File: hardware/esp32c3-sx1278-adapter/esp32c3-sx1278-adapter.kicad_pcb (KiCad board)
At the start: 2 copper layers, 24 x 58 mm, 5 parts, among them J1 Conn_01x08, J2 Conn_01x08, J3 Antenna, J4 SMA, U2 SX1278_module

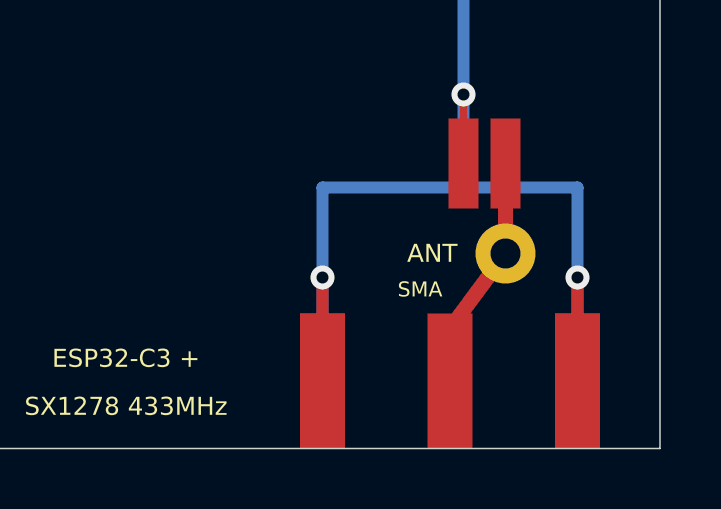
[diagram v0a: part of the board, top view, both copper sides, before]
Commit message: Add the green D-Sun CC1101 board with the same assets as the blue E07-M1101D
The user's second CC1101 board ("433MHz D-Sun CC1101", green; EasyEDA calls
it RF1101SE V3.1) carries the same eight signals on the same 2x4 header,
with the GND/VCC column in the same place but the three signal columns
permuted, so it does not fit the socket adapter's pinout and is supported
with jumper wires instead.

* scripts/generate_dsun.py -> hardware/parts/cc1101-dsun: outline 14.4 x
  30, header rows 2.1 / 4.6 from the edge, columns 2.9..10.5 from the left
  long edge, two 1.8 mm holes beside the SMA jack, pin names on both sides
  and the original's back-side legend grid.  Dimensions measured from the
  user's photos with the E07-M1101D as the scale (+/- 0.3 mm).
* 3D models (cc1101-dsun.step, -components.step) attached to the board.
* Pinout diagram: third column, green, with the back legend; wiring diagram
  docs/images/wiring-cc1101-dsun.svg (its wires cannot all nest; the chip
  select runs along the back of the board below the header).
* README: comparison table with the blue board, why the socket does not
  take it, a component-board section, 3D model row; CI regenerates it and
  the manufacturing notes cover it.

The photos also showed both boards' edge-mount SMA jacks have their ground
legs 5.5 mm apart, not 8.5: the shared SMA footprint, the E07 reference
board, the SX1278 adapter's SMA ground routing (now skirting the antenna
wire hole) and the 3D jack model follow.

Strap change for the jumper-wire builds: the SuperMini has one G pin (the
brown wire's), so the Ra-02's strap wire goes from GPIO5 to GPIO4, which
firmware drives low while reading the strap; documented with the read
procedure.

Co-Authored-By: Claude Fable 5.1 <noreply@anthropic.com>
Claude-Session: https://claude.ai/code/session_01JoGdh4Cg3VtTTDZi4gQuiN
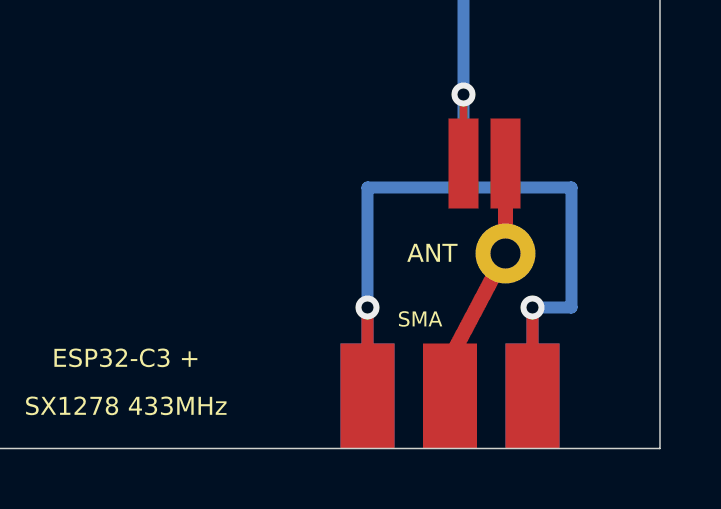
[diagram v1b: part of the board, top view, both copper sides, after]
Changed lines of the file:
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@@
 		(sheetfile "esp32c3-sx1278-adapter.kicad_sch")
 		(property "Reference" "J4"
-			(at 0 -5.5 0)
+			(at 0 -4.5 0)
 			(layer "F.SilkS")
 			(hide yes)
@@
 		(attr smd)
 		(fp_rect
-			(start -5.25 -4.75)
-			(end 5.25 0.25)
+			(start -3.9 -3.75)
+			(end 3.9 0.25)
 			(stroke
 				(width 0.05)
@@
 		)
 		(fp_text user "${REFERENCE}"
-			(at 0 -5.5 0)
+			(at 0 -4.5 0)
 			(layer "F.Fab")
 			(effects
@@
 		)
 		(pad "1" smd rect
-			(at 0 -2.25)
-			(size 1.5 4.5)
+			(at 0 -1.75)
+			(size 1.8 3.5)
 			(layers "F.Cu" "F.Mask" "F.Paste")
 			(net 20 "ANT")
@@
 		)
 		(pad "2" smd rect
-			(at -4.25 -2.25)
-			(size 1.5 4.5)
+			(at -2.75 -1.75)
+			(size 1.8 3.5)
 			(layers "F.Cu" "F.Mask" "F.Paste")
 			(net 10 "GND")
@@
 		)
 		(pad "2" smd rect
-			(at -4.25 -2.25)
-			(size 1.5 4.5)
+			(at -2.75 -1.75)
+			(size 1.8 3.5)
 			(layers "B.Cu" "B.Mask" "B.Paste")
 			(net 10 "GND")
@@
 		)
 		(pad "2" smd rect
-			(at 4.25 -2.25)
-			(size 1.5 4.5)
+			(at 2.75 -1.75)
+			(size 1.8 3.5)
 			(layers "F.Cu" "F.Mask" "F.Paste")
 			(net 10 "GND")
@@
 		)
 		(pad "2" smd rect
-			(at 4.25 -2.25)
-			(size 1.5 4.5)
+			(at 2.75 -1.75)
+			(size 1.8 3.5)
 			(layers "B.Cu" "B.Mask" "B.Paste")
 			(net 10 "GND")
@@
 	)
 	(gr_text "SMA"
-		(at 116 152.7 0)
+		(at 116 153.7 0)
 		(layer "F.SilkS")
 		(effects
@@
 	(segment
 		(start 118.85 151.5)
-		(end 117 154)
+		(end 117 155)
 		(width 0.5)
 		(layer "F.Cu")
@@
 	)
 	(segment
-		(start 117 154)
-		(end 117 155.75)
+		(start 117 155)
+		(end 117 156.25)
 		(width 0.5)
 		(layer "F.Cu")
@@
 	(segment
 		(start 117.45 149.3)
-		(end 121.25 149.3)
-		(width 0.4)
-		(layer "B.Cu")
-		(net 10)
-	)
-	(segment
-		(start 121.25 149.3)
-		(end 121.25 155.75)
+		(end 121.05 149.3)
+		(width 0.4)
+		(layer "B.Cu")
+		(net 10)
+	)
+	(segment
+		(start 121.05 149.3)
+		(end 121.05 153.3)
+		(width 0.4)
+		(layer "B.Cu")
+		(net 10)
+	)
+	(segment
+		(start 121.05 153.3)
+		(end 119.75 153.3)
+		(width 0.4)
+		(layer "B.Cu")
+		(net 10)
+	)
+	(segment
+		(start 119.75 153.3)
+		(end 119.75 156.25)
 		(width 0.4)
 		(layer "B.Cu")
@@
 	(segment
 		(start 117.45 149.3)
-		(end 112.75 149.3)
-		(width 0.4)
-		(layer "B.Cu")
-		(net 10)
-	)
-	(segment
-		(start 112.75 149.3)
-		(end 112.75 155.75)
-		(width 0.4)
-		(layer "B.Cu")
-		(net 10)
-	)
-	(segment
-		(start 112.75 152.3)
-		(end 112.75 155.75)
-		(width 0.4)
-		(layer "F.Cu")
-		(net 10)
-	)
-	(segment
-		(start 121.25 152.3)
-		(end 121.25 155.75)
+		(end 114.25 149.3)
+		(width 0.4)
+		(layer "B.Cu")
+		(net 10)
+	)
+	(segment
+		(start 114.25 149.3)
+		(end 114.25 156.25)
+		(width 0.4)
+		(layer "B.Cu")
+		(net 10)
+	)
+	(segment
+		(start 114.25 153.3)
+		(end 114.25 156.25)
+		(width 0.4)
+		(layer "F.Cu")
+		(net 10)
+	)
+	(segment
+		(start 119.75 153.3)
+		(end 119.75 156.25)
 		(width 0.4)
 		(layer "F.Cu")
@@
 	)
 	(via
-		(at 112.75 152.3)
+		(at 114.25 153.3)
 		(size 0.8)
 		(drill 0.4)
@@
 	)
 	(via
-		(at 121.25 152.3)
+		(at 119.75 153.3)
 		(size 0.8)
 		(drill 0.4)

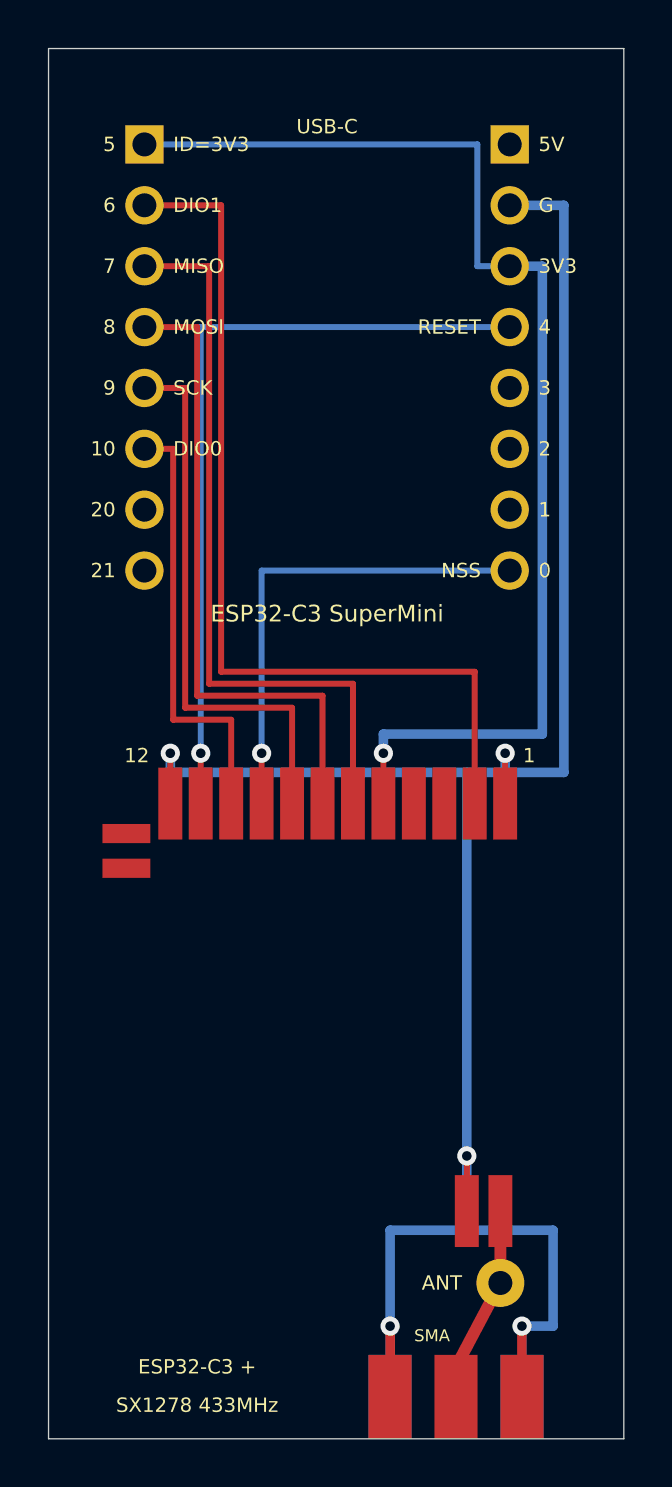
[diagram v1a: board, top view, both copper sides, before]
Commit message: Adapters: GPIO map that lets the same socket take all three radio boards
The green D-Sun CC1101 board plugs into the socket adapter's 2x4 socket
too; only its signal order differs, which the firmware absorbs with a pin
map per board.  What the hardware must guarantee is that no socket
position that carries a radio OUTPUT on any of the boards is an ESP32-C3
boot strapping pin (GPIO2/8/9).  Only position 4 (blue CSN, green SCK,
Ra-02 NSS) is an input on every board, so it takes GPIO9; GPIO8 moves to
the spare header and positions 5 and 6 are fed from GPIO3 and GPIO4.

Socket positions 3..8 are now GPIO10, 9, 3, 4, 7, 6.  Per-board maps:
blue E07 MOSI 4 SCK 3 CSN 9 MISO 7 GDO0 10 GDO2 6; green D-Sun MOSI 10
SCK 9 CSN 6 MISO 3 GDO0 7 GDO2 4; Ra-02 MOSI 4 SCK 3 NSS 9 MISO 7 RST 10
DIO0 6.  The README also describes telling the two CC1101 boards apart
passively at power-up (an unconfigured CC1101 clocks XOSC/192 out of
GDO0, on GPIO10 for the blue board and GPIO7 for the green).

Socket adapter routing, still entirely on the back copper: GPIO9 leaves
its pad sideways into the gap before GPIO10 and drops into position 4;
MISO takes the column under GPIO8's pad; SCK and MOSI come down from the
power row through the gaps either side of GPIO8's pad, and GPIO8 climbs
between them to the header (now 3V3, 8, 2, 1, 0, 21TX, 20RX).

SX1278 module adapter: same GPIOs with MOSI and SCK swapped (GPIO3/4) so
its bottom copper nests, NSS on GPIO9 via the top-copper bus, RESET on
GPIO8 (an ESP32 output).

Jumper-wire diagrams: one layout serves all three boards; GPIO4 and GPIO3
take the ribbon's white and black; the Ra-02 strap goes to GPIO1 (GPIO4
is now MOSI).  Both adapters pass ERC and DRC.

Co-Authored-By: Claude Fable 5.1 <noreply@anthropic.com>
Claude-Session: https://claude.ai/code/session_01JoGdh4Cg3VtTTDZi4gQuiN
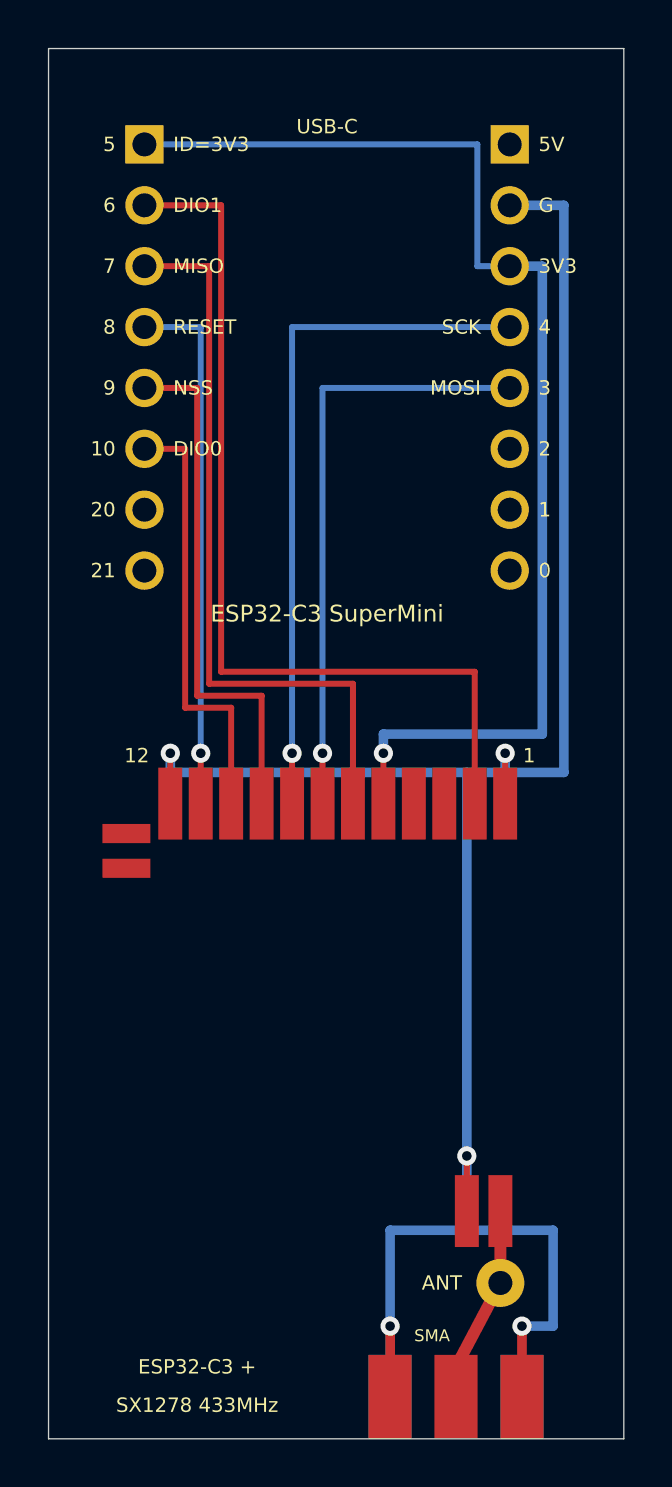
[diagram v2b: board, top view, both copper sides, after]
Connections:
- J1 pad 4: MOSI -> RESET
- J1 pad 5: SCK -> NSS
- J2 pad 4: RESET -> SCK
- J2 pad 5: GPIO3 -> MOSI
- J2 pad 8: NSS -> GPIO0
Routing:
- net RESET: track 33.3 -> 22.7 mm
- net SCK: track 24.0 -> 29.5 mm, vias 0 -> 1
- net NSS: track 20.6 -> 22.7 mm, vias 1 -> 0
- net MOSI: track 27.8 -> 25.6 mm, vias 0 -> 1
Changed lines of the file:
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@@
 	(net 2 "DIO1")
 	(net 3 "MISO")
-	(net 4 "MOSI")
-	(net 5 "SCK")
+	(net 4 "RESET")
+	(net 5 "NSS")
 	(net 6 "DIO0")
 	(net 7 "GPIO20")
@@
 	(net 9 "+5V")
 	(net 10 "GND")
-	(net 11 "RESET")
-	(net 12 "GPIO3")
+	(net 11 "SCK")
+	(net 12 "MOSI")
 	(net 13 "GPIO2")
 	(net 14 "GPIO1")
-	(net 15 "NSS")
+	(net 15 "GPIO0")
 	(net 16 "DIO2")
 	(net 17 "DIO3")
@@
 			(layers "*.Cu" "*.Mask")
 			(remove_unused_layers no)
-			(net 4 "MOSI")
+			(net 4 "RESET")
 			(pinfunction "Pin_4")
 			(pintype "passive")
@@
 			(layers "*.Cu" "*.Mask")
 			(remove_unused_layers no)
-			(net 5 "SCK")
+			(net 5 "NSS")
 			(pinfunction "Pin_5")
 			(pintype "passive")
@@
 			(layers "*.Cu" "*.Mask")
 			(remove_unused_layers no)
-			(net 11 "RESET")
+			(net 11 "SCK")
 			(pinfunction "Pin_4")
 			(pintype "passive")
@@
 			(layers "*.Cu" "*.Mask")
 			(remove_unused_layers no)
-			(net 12 "GPIO3")
+			(net 12 "MOSI")
 			(pinfunction "Pin_5")
 			(pintype "passive")
@@
 			(layers "*.Cu" "*.Mask")
 			(remove_unused_layers no)
-			(net 15 "NSS")
+			(net 15 "GPIO0")
 			(pinfunction "Pin_8")
 			(pintype "passive")
@@
 			(size 1 3)
 			(layers "F.Cu" "F.Mask" "F.Paste")
-			(net 4 "MOSI")
+			(net 12 "MOSI")
 			(pinfunction "Pin_7")
 			(pintype "passive")
@@
 			(size 1 3)
 			(layers "F.Cu" "F.Mask" "F.Paste")
-			(net 5 "SCK")
+			(net 11 "SCK")
 			(pinfunction "Pin_8")
 			(pintype "passive")
@@
 			(size 1 3)
 			(layers "F.Cu" "F.Mask" "F.Paste")
-			(net 15 "NSS")
+			(net 5 "NSS")
 			(pinfunction "Pin_9")
 			(pintype "passive")
@@
 			(size 1 3)
 			(layers "F.Cu" "F.Mask" "F.Paste")
-			(net 11 "RESET")
+			(net 4 "RESET")
 			(pinfunction "Pin_11")
 			(pintype "passive")
@@
 		)
 	)
-	(gr_text "MOSI"
+	(gr_text "RESET"
 		(at 105.2 111.62 0)
 		(layer "F.SilkS")
@@
 		)
 	)
-	(gr_text "SCK"
+	(gr_text "NSS"
 		(at 105.2 114.16 0)
 		(layer "F.SilkS")
@@
 		)
 	)
-	(gr_text "RESET"
+	(gr_text "SCK"
 		(at 118.04 111.62 0)
 		(layer "F.SilkS")
@@
 		)
 	)
+	(gr_text "MOSI"
+		(at 118.04 114.16 0)
+		(layer "F.SilkS")
+		(effects
+			(font
+				(size 0.6 0.6)
+				(thickness 0.09)
+			)
+			(justify right)
+		)
+	)
 	(gr_text "2"
 		(at 120.44 116.7 0)
@@
 		)
 	)
-	(gr_text "NSS"
-		(at 118.04 121.78 0)
-		(layer "F.SilkS")
-		(effects
-			(font
-				(size 0.6 0.6)
-				(thickness 0.09)
-			)
-			(justify right)
-		)
-	)
 	(gr_text "ANT"
 		(at 117.25 151.5 0)
@@
 	)
 	(segment
-		(start 104 111.62)
-		(end 106.2 111.62)
-		(width 0.25)
-		(layer "F.Cu")
-		(net 4)
-	)
-	(segment
-		(start 106.2 111.62)
+		(start 104 114.16)
+		(end 106.2 114.16)
+		(width 0.25)
+		(layer "F.Cu")
+		(net 5)
+	)
+	(segment
+		(start 106.2 114.16)
 		(end 106.2 127)
 		(width 0.25)
 		(layer "F.Cu")
-		(net 4)
+		(net 5)
 	)
 	(segment
 		(start 106.2 127)
-		(end 111.43 127)
-		(width 0.25)
-		(layer "F.Cu")
-		(net 4)
-	)
-	(segment
-		(start 111.43 127)
-		(end 111.43 132)
-		(width 0.25)
-		(layer "F.Cu")
-		(net 4)
-	)
-	(segment
-		(start 104 114.16)
-		(end 105.7 114.16)
+		(end 108.89 127)
 		(width 0.25)
 		(layer "F.Cu")
@@
 	)
 	(segment
-		(start 105.7 114.16)
+		(start 108.89 127)
+		(end 108.89 132)
+		(width 0.25)
+		(layer "F.Cu")
+		(net 5)
+	)
+	(segment
+		(start 104 116.7)
+		(end 105.7 116.7)
+		(width 0.25)
+		(layer "F.Cu")
+		(net 6)
+	)
+	(segment
+		(start 105.7 116.7)
 		(end 105.7 127.5)
 		(width 0.25)
 		(layer "F.Cu")
-		(net 5)
+		(net 6)
 	)
 	(segment
 		(start 105.7 127.5)
-		(end 110.16 127.5)
-		(width 0.25)
-		(layer "F.Cu")
-		(net 5)
-	)
-	(segment
-		(start 110.16 127.5)
-		(end 110.16 132)
-		(width 0.25)
-		(layer "F.Cu")
-		(net 5)
-	)
-	(segment
-		(start 104 116.7)
-		(end 105.2 116.7)
+		(end 107.62 127.5)
 		(width 0.25)
 		(layer "F.Cu")
@@
 	)
 	(segment
-		(start 105.2 116.7)
-		(end 105.2 128)
-		(width 0.25)
-		(layer "F.Cu")
-		(net 6)
-	)
-	(segment
-		(start 105.2 128)
-		(end 107.62 128)
-		(width 0.25)
-		(layer "F.Cu")
-		(net 6)
-	)
-	(segment
-		(start 107.62 128)
+		(start 107.62 127.5)
 		(end 107.62 132)
 		(width 0.25)
@@
 	)
 	(segment
-		(start 119.24 111.62)
+		(start 104 111.62)
 		(end 106.35 111.62)
 		(width 0.25)
 		(layer "B.Cu")
-		(net 11)
+		(net 4)
 	)
 	(segment
@@
 		(width 0.25)
 		(layer "B.Cu")
-		(net 11)
+		(net 4)
 	)
 	(segment
@@
 		(width 0.25)
 		(layer "F.Cu")
+		(net 4)
+	)
+	(segment
+		(start 119.24 111.62)
+		(end 110.16 111.62)
+		(width 0.25)
+		(layer "B.Cu")
 		(net 11)
 	)
 	(segment
-		(start 119.24 121.78)
-		(end 108.89 121.78)
-		(width 0.25)
-		(layer "B.Cu")
-		(net 15)
-	)
-	(segment
-		(start 108.89 121.78)
-		(end 108.89 129.4)
-		(width 0.25)
-		(layer "B.Cu")
-		(net 15)
-	)
-	(segment
-		(start 108.89 129.4)
-		(end 108.89 132)
-		(width 0.25)
-		(layer "F.Cu")
-		(net 15)
+		(start 110.16 111.62)
+		(end 110.16 129.4)
+		(width 0.25)
+		(layer "B.Cu")
+		(net 11)
+	)
+	(segment
+		(start 110.16 129.4)
+		(end 110.16 132)
+		(width 0.25)
+		(layer "F.Cu")
+		(net 11)
+	)
+	(segment
+		(start 119.24 114.16)
+		(end 111.43 114.16)
+		(width 0.25)
+		(layer "B.Cu")
+		(net 12)
+	)
+	(segment
+		(start 111.43 114.16)
+		(end 111.43 129.4)
+		(width 0.25)
+		(layer "B.Cu")
+		(net 12)
+	)
+	(segment
+		(start 111.43 129.4)
+		(end 111.43 132)
+		(width 0.25)
+		(layer "F.Cu")
+		(net 12)
 	)
 	(segment
@@
 		(drill 0.4)
 		(layers "F.Cu" "B.Cu")
-		(net 11)
+		(net 4)
 	)
 	(via
-		(at 108.89 129.4)
+		(at 110.16 129.4)
 		(size 0.8)
 		(drill 0.4)
 		(layers "F.Cu" "B.Cu")
-		(net 15)
+		(net 11)
 	)
 	(via
+		(at 111.43 129.4)
+		(size 0.8)
+		(drill 0.4)
+		(layers "F.Cu" "B.Cu")
+		(net 12)
+	)
+	(via
